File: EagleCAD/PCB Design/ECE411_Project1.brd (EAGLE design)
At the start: 160 x 100 mm, 23 parts

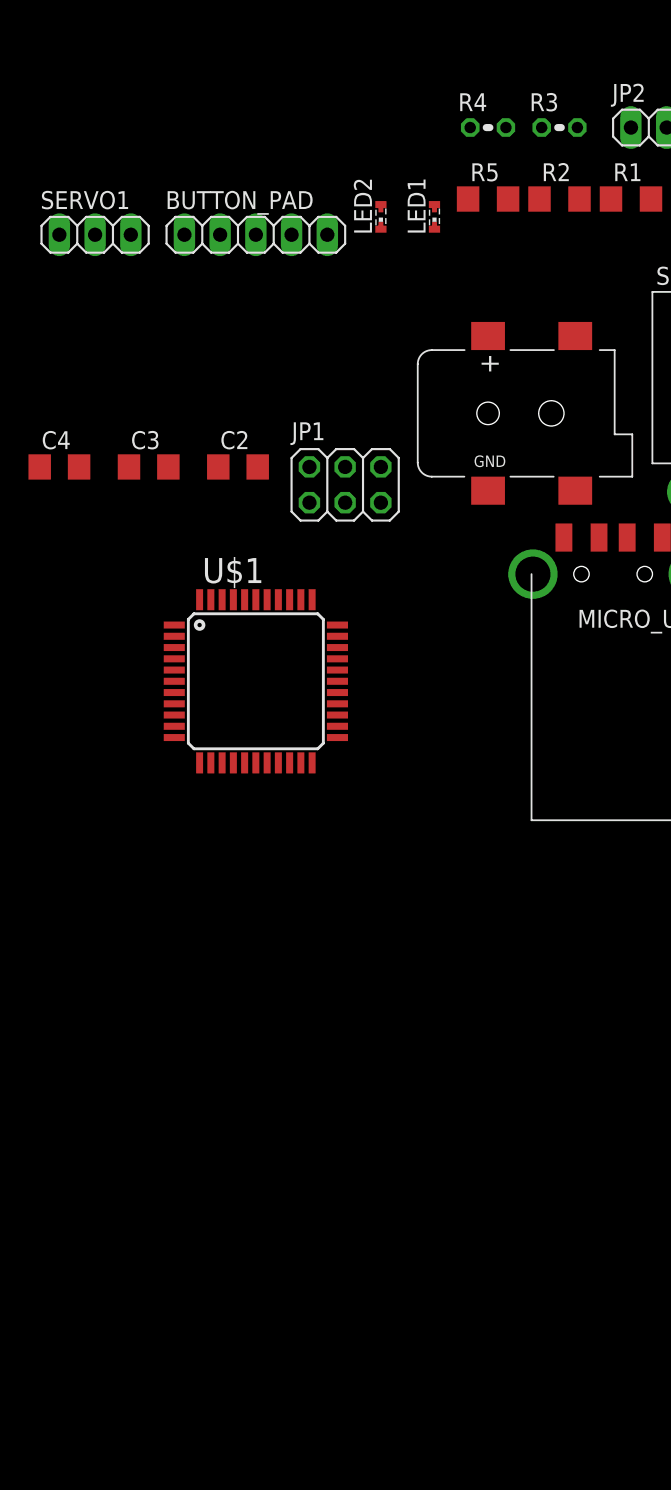
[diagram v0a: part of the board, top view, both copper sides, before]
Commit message: Made Xtal library file
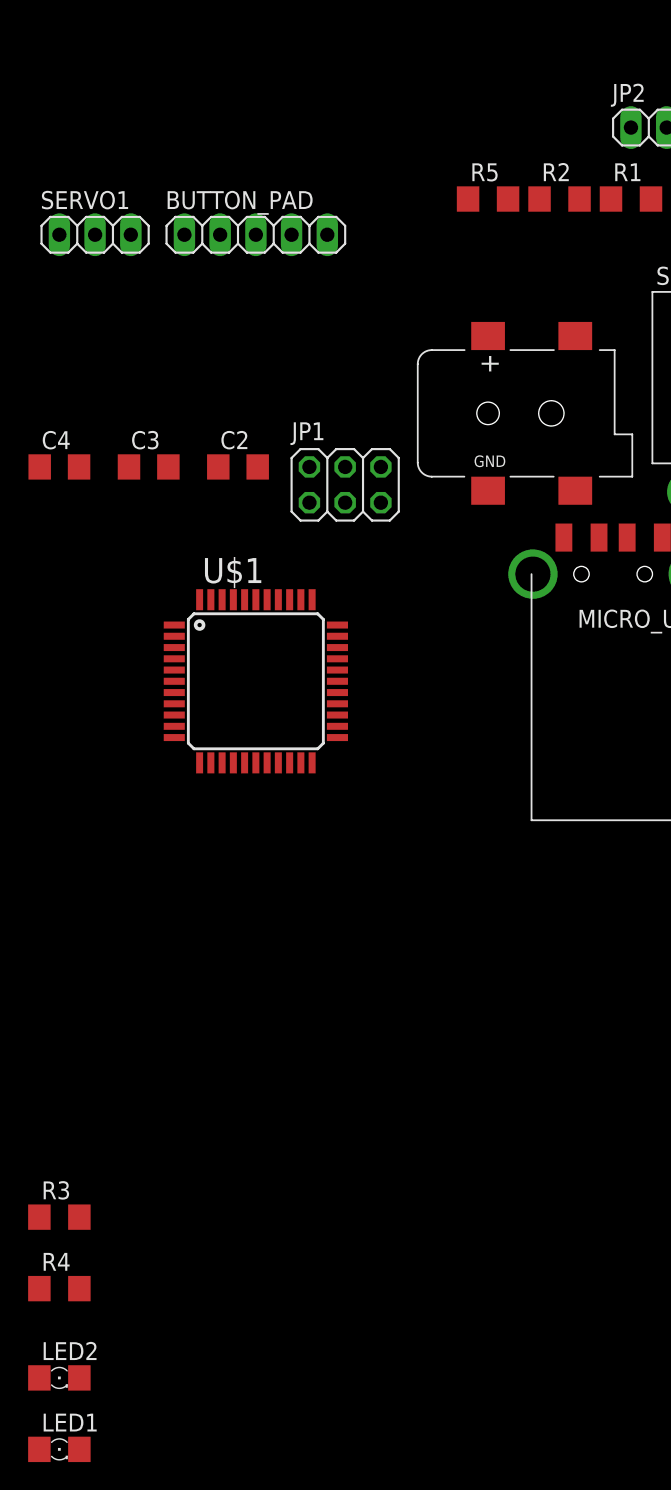
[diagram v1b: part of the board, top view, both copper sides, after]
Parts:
- LED1, LED2: device adafruit:SMARTLED-TTW -> led:1206
- R3, R4: value (none) -> 1k; device rcl:0204V -> rcl:R1206
- moved LED1 91.6 mm to (-67.3, -20.3)
- moved R4 88.0 mm to (-67.3, -8.89)
- moved LED2 85.7 mm to (-67.3, -15.2)
- moved R3 85.2 mm to (-67.3, -3.81)
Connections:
- net GND: now also LED1.C, LED2.C; no longer LED1.C@1, LED2.C@1
- net N$10: now also LED1.A, R4.1; no longer LED1.A@1, R3.2
- net N$6: now also R3.2; no longer R4.1
- net N$8: now also R4.2; no longer R3.1
- net N$9: now also LED2.A, R3.1; no longer LED2.A@1, R4.2
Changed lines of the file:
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@@
 <element name="JP1" library="pinhead" library_urn="urn:adsk.eagle:library:325" package="2X03" package3d_urn="urn:adsk.eagle:package:22462/2" value="" x="-46.99" y="48.26"/>
 <element name="JP2" library="pinhead" library_urn="urn:adsk.eagle:library:325" package="1X02" package3d_urn="urn:adsk.eagle:package:22435/2" value="" x="-25.4" y="73.66"/>
-<element name="LED1" library="adafruit" package="SMARTLED-TTW" value="" x="-40.64" y="67.31"/>
-<element name="LED2" library="adafruit" package="SMARTLED-TTW" value="" x="-44.45" y="67.31"/>
 <element name="MICRO_USB_TYPE_B" library="adafruit" package="MOLEX_480371000" value="USB-A" x="-27.94" y="41.91">
 <attribute name="SPICEPREFIX" value="X" x="-27.94" y="41.91" size="1.778" layer="27" display="off"/>
@@
 <attribute name="SPICEPREFIX" value="R" x="-31.75" y="68.58" size="1.778" layer="27" display="off"/>
 </element>
-<element name="R3" library="rcl" library_urn="urn:adsk.eagle:library:334" package="0204V" package3d_urn="urn:adsk.eagle:package:23495/1" value="" x="-31.75" y="73.66">
-<attribute name="SPICEPREFIX" value="2.2k" x="-31.75" y="73.66" size="1.778" layer="27" display="off"/>
-</element>
-<element name="R4" library="rcl" library_urn="urn:adsk.eagle:library:334" package="0204V" package3d_urn="urn:adsk.eagle:package:23495/1" value="" x="-36.83" y="73.66">
-<attribute name="SPICEPREFIX" value="2.2k" x="-36.83" y="73.66" size="1.778" layer="27" display="off"/>
-</element>
 <element name="R5" library="rcl" library_urn="urn:adsk.eagle:library:334" package="R1206" package3d_urn="urn:adsk.eagle:package:23540/2" value="10k" x="-36.83" y="68.58">
 <attribute name="SPICEPREFIX" value="R" x="-36.83" y="68.58" size="1.778" layer="27" display="off"/>
@@
 <element name="SERVO2" library="pinhead" library_urn="urn:adsk.eagle:library:325" package="1X03" package3d_urn="urn:adsk.eagle:package:22458/2" value="" x="-17.78" y="73.66"/>
 <element name="U$1" library="adafruit" package="TQFP44" value="ATMEGA32U4-AU" x="-53.34" y="34.29"/>
+<element name="R3" library="rcl" library_urn="urn:adsk.eagle:library:334" package="R1206" package3d_urn="urn:adsk.eagle:package:23540/2" value="1k" x="-67.31" y="-3.81">
+<attribute name="SPICEPREFIX" value="R" x="-67.31" y="-3.81" size="1.778" layer="27" display="off"/>
+</element>
+<element name="R4" library="rcl" library_urn="urn:adsk.eagle:library:334" package="R1206" package3d_urn="urn:adsk.eagle:package:23540/2" value="1k" x="-67.31" y="-8.89">
+<attribute name="SPICEPREFIX" value="R" x="-67.31" y="-8.89" size="1.778" layer="27" display="off"/>
+</element>
+<element name="LED2" library="led" library_urn="urn:adsk.eagle:library:259" package="1206" package3d_urn="urn:adsk.eagle:package:15796/1" value="" x="-67.31" y="-15.24"/>
+<element name="LED1" library="led" library_urn="urn:adsk.eagle:library:259" package="1206" package3d_urn="urn:adsk.eagle:package:15796/1" value="" x="-67.31" y="-20.32"/>
 </elements>
 <signals>
@@
 <contactref element="U$1" pad="5"/>
 <contactref element="C1" pad="2"/>
-<contactref element="LED2" pad="C@1"/>
-<contactref element="LED1" pad="C@1"/>
 <contactref element="SERVO2" pad="3"/>
 <contactref element="S1" pad="P"/>
@@
 <contactref element="C4" pad="2"/>
 <contactref element="C5" pad="2"/>
-<wire x1="-15.11" y1="68.58" x2="-15.24" y2="73.66" width="0" layer="19" extent="1-1"/>
+<contactref element="LED2" pad="C"/>
+<contactref element="LED1" pad="C"/>
+<wire x1="148.59" y1="3.81" x2="147.32" y2="63.5" width="0" layer="19" extent="1-1"/>
+<wire x1="-15.11" y1="68.58" x2="147.32" y2="63.5" width="0" layer="19" extent="1-1"/>
+<wire x1="-15.24" y1="73.66" x2="-15.11" y2="68.58" width="0" layer="19" extent="1-1"/>
 <wire x1="-20.19" y1="68.58" x2="-15.11" y2="68.58" width="0" layer="19" extent="1-1"/>
-<wire x1="-40.64" y1="67.81" x2="-20.19" y2="68.58" width="0" layer="19" extent="1-1"/>
-<wire x1="-44.45" y1="67.81" x2="-40.64" y2="67.81" width="0" layer="19" extent="1-1"/>
-<wire x1="-48.26" y1="66.04" x2="-44.45" y2="67.81" width="0" layer="19" extent="1-1"/>
-<wire x1="-62.23" y1="66.04" x2="-48.26" y2="66.04" width="0" layer="19" extent="1-1"/>
-<wire x1="-59.56" y1="49.53" x2="-62.23" y2="66.04" width="0" layer="19" extent="1-1"/>
+<wire x1="-15.494" y1="47.752" x2="-15.11" y2="68.58" width="0" layer="19" extent="1-1"/>
+<wire x1="-30.63" y1="47.84" x2="-15.494" y2="47.752" width="0" layer="19" extent="1-1"/>
+<wire x1="-31.44" y1="44.51" x2="-30.63" y2="47.84" width="0" layer="19" extent="1-1"/>
+<wire x1="-44.45" y1="49.53" x2="-30.63" y2="47.84" width="0" layer="19" extent="1-1"/>
+<wire x1="-53.21" y1="49.53" x2="-44.45" y2="49.53" width="0" layer="19" extent="1-1"/>
+<wire x1="-59.56" y1="49.53" x2="-53.21" y2="49.53" width="0" layer="19" extent="1-1"/>
 <wire x1="-65.91" y1="49.53" x2="-59.56" y2="49.53" width="0" layer="19" extent="1-1"/>
-<wire x1="-53.21" y1="49.53" x2="-59.56" y2="49.53" width="0" layer="19" extent="1-1"/>
-<wire x1="-44.45" y1="49.53" x2="-53.21" y2="49.53" width="0" layer="19" extent="1-1"/>
 <wire x1="-56.54" y1="40.09" x2="-59.56" y2="49.53" width="0" layer="19" extent="1-1"/>
 <wire x1="-59.14" y1="35.09" x2="-56.54" y2="40.09" width="0" layer="19" extent="1-1"/>
@@
 <wire x1="-54.94" y1="28.49" x2="-59.14" y2="35.09" width="0" layer="19" extent="1-1"/>
 <wire x1="-47.54" y1="30.29" x2="-54.94" y2="28.49" width="0" layer="19" extent="1-1"/>
-<wire x1="-30.63" y1="47.84" x2="-44.45" y2="49.53" width="0" layer="19" extent="1-1"/>
-<wire x1="-31.44" y1="44.51" x2="-30.63" y2="47.84" width="0" layer="19" extent="1-1"/>
-<wire x1="-15.494" y1="47.752" x2="-30.63" y2="47.84" width="0" layer="19" extent="1-1"/>
-<wire x1="147.32" y1="63.5" x2="-54.94" y2="28.49" width="0" layer="19" extent="1-1"/>
-<wire x1="148.59" y1="3.81" x2="147.32" y2="63.5" width="0" layer="19" extent="1-1"/>
+<wire x1="-62.23" y1="66.04" x2="-59.56" y2="49.53" width="0" layer="19" extent="1-1"/>
+<wire x1="-48.26" y1="66.04" x2="-62.23" y2="66.04" width="0" layer="19" extent="1-1"/>
+<wire x1="-65.888" y1="-15.24" x2="-54.94" y2="28.49" width="0" layer="19" extent="1-1"/>
+<wire x1="-65.888" y1="-20.32" x2="-65.888" y2="-15.24" width="0" layer="19" extent="1-1"/>
 </signal>
 <signal name="+3V3">
@@
 <signal name="N$6">
 <contactref element="U$1" pad="18"/>
-<contactref element="R4" pad="1"/>
-<wire x1="-52.54" y1="28.49" x2="-38.1" y2="73.66" width="0" layer="19" extent="1-1"/>
+<contactref element="R3" pad="2"/>
+<wire x1="-52.54" y1="28.49" x2="-65.888" y2="-3.81" width="0" layer="19" extent="1-1"/>
 </signal>
 <signal name="N$9">
-<contactref element="R4" pad="2"/>
-<contactref element="LED2" pad="A@1"/>
-<wire x1="-44.45" y1="66.81" x2="-35.56" y2="73.66" width="0" layer="19" extent="1-1"/>
+<contactref element="R3" pad="1"/>
+<contactref element="LED2" pad="A"/>
+<wire x1="-68.732" y1="-3.81" x2="-68.732" y2="-15.24" width="0" layer="19" extent="1-1"/>
 </signal>
 <signal name="N$10">
-<contactref element="R3" pad="2"/>
-<contactref element="LED1" pad="A@1"/>
-<wire x1="-40.64" y1="66.81" x2="-30.48" y2="73.66" width="0" layer="19" extent="1-1"/>
+<contactref element="R4" pad="1"/>
+<contactref element="LED1" pad="A"/>
+<wire x1="-68.732" y1="-8.89" x2="-68.732" y2="-20.32" width="0" layer="19" extent="1-1"/>
 </signal>
 <signal name="VCC">
@@
 </signal>
 <signal name="N$8">
-<contactref element="R3" pad="1"/>
 <contactref element="U$1" pad="19"/>
-<wire x1="-51.74" y1="28.49" x2="-33.02" y2="73.66" width="0" layer="19" extent="1-1"/>
+<contactref element="R4" pad="2"/>
+<wire x1="-51.74" y1="28.49" x2="-65.888" y2="-8.89" width="0" layer="19" extent="1-1"/>
 </signal>
 <signal name="N$7">
